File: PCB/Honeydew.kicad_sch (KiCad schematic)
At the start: 12 parts

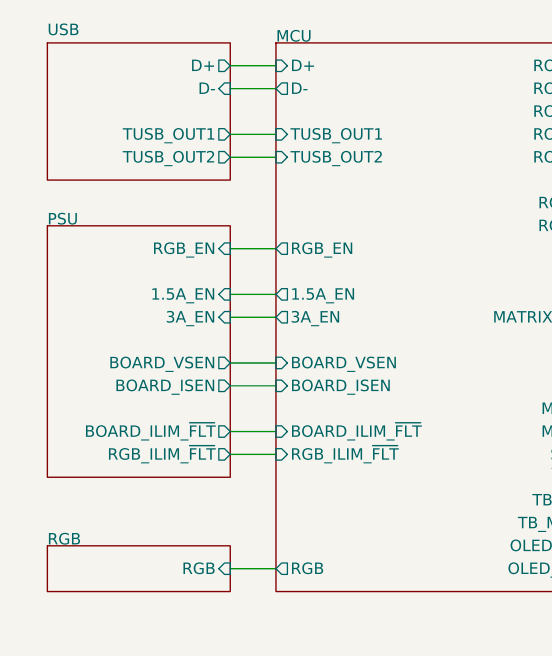
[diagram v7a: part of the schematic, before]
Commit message: Finished routing RGB LEDs.
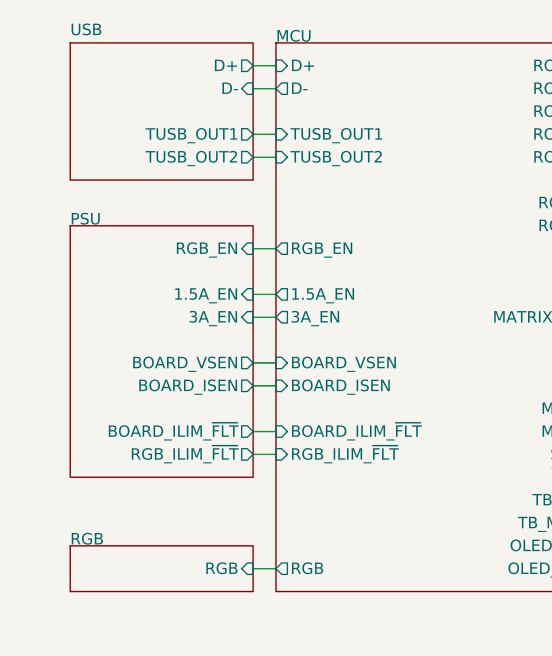
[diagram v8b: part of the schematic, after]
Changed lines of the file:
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@@
     (stroke (width 0) (type default))
   )
-  (wire (pts (xy 38.1 60.96) (xy 43.18 60.96))
+  (wire (pts (xy 40.64 60.96) (xy 43.18 60.96))
     (stroke (width 0) (type default))
   )
@@
     (stroke (width 0) (type default))
   )
-  (wire (pts (xy 38.1 76.2) (xy 43.18 76.2))
+  (wire (pts (xy 40.64 76.2) (xy 43.18 76.2))
     (stroke (width 0) (type default))
   )
@@
     (stroke (width 0) (type default))
   )
-  (wire (pts (xy 43.18 40.64) (xy 38.1 40.64))
+  (wire (pts (xy 43.18 40.64) (xy 40.64 40.64))
     (stroke (width 0) (type default))
   )
@@
     (stroke (width 0) (type default))
   )
-  (wire (pts (xy 43.18 20.32) (xy 38.1 20.32))
+  (wire (pts (xy 43.18 20.32) (xy 40.64 20.32))
     (stroke (width 0) (type default))
   )
@@
     (stroke (width 0) (type default))
   )
-  (wire (pts (xy 43.18 27.94) (xy 38.1 27.94))
+  (wire (pts (xy 43.18 27.94) (xy 40.64 27.94))
     (stroke (width 0) (type default))
   )
@@
     (stroke (width 0) (type default))
   )
-  (wire (pts (xy 38.1 48.26) (xy 43.18 48.26))
-    (stroke (width 0) (type default))
-  )
-  (wire (pts (xy 43.18 45.72) (xy 38.1 45.72))
-    (stroke (width 0) (type default))
-  )
-  (wire (pts (xy 38.1 22.86) (xy 43.18 22.86))
+  (wire (pts (xy 40.64 48.26) (xy 43.18 48.26))
+    (stroke (width 0) (type default))
+  )
+  (wire (pts (xy 43.18 45.72) (xy 40.64 45.72))
+    (stroke (width 0) (type default))
+  )
+  (wire (pts (xy 40.64 22.86) (xy 43.18 22.86))
     (stroke (width 0) (type default))
   )
@@
     (stroke (width 0) (type default))
   )
-  (wire (pts (xy 43.18 53.34) (xy 38.1 53.34))
-    (stroke (width 0) (type default))
-  )
-  (wire (pts (xy 38.1 63.5) (xy 43.18 63.5))
+  (wire (pts (xy 43.18 53.34) (xy 40.64 53.34))
+    (stroke (width 0) (type default))
+  )
+  (wire (pts (xy 40.64 63.5) (xy 43.18 63.5))
     (stroke (width 0) (type default))
   )
@@
     (stroke (width 0) (type default))
   )
-  (wire (pts (xy 38.1 30.48) (xy 43.18 30.48))
-    (stroke (width 0) (type default))
-  )
-  (wire (pts (xy 38.1 55.88) (xy 43.18 55.88))
+  (wire (pts (xy 40.64 30.48) (xy 43.18 30.48))
+    (stroke (width 0) (type default))
+  )
+  (wire (pts (xy 40.64 55.88) (xy 43.18 55.88))
     (stroke (width 0) (type default))
   )
@@
     )
   )
-  (sheet (at 17.78 17.78) (size 20.32 15.24) (fields_autoplaced)
+  (sheet (at 20.32 17.78) (size 20.32 15.24) (fields_autoplaced)
     (stroke (width 0.1524) (type solid))
     (fill (color 0 0 0 0.0000))
-    (property "Sheetname" "USB" (at 17.78 17.0684 0)
+    (property "Sheetname" "USB" (at 20.32 17.0684 0)
       (effects (font (size 1.27 1.27)) (justify left bottom))
     )
-    (property "Sheetfile" "USB.kicad_sch" (at 17.78 33.6046 0)
+    (property "Sheetfile" "USB.kicad_sch" (at 20.32 33.6046 0)
       (effects (font (size 1.27 1.27)) (justify left top) hide)
     )
-    (pin "D-" input (at 38.1 22.86 0)
-      (effects (font (size 1.27 1.27)) (justify right))
-    )
-    (pin "D+" output (at 38.1 20.32 0)
-      (effects (font (size 1.27 1.27)) (justify right))
-    )
-    (pin "TUSB_OUT1" output (at 38.1 27.94 0)
-      (effects (font (size 1.27 1.27)) (justify right))
-    )
-    (pin "TUSB_OUT2" output (at 38.1 30.48 0)
+    (pin "D-" input (at 40.64 22.86 0)
+      (effects (font (size 1.27 1.27)) (justify right))
+    )
+    (pin "D+" output (at 40.64 20.32 0)
+      (effects (font (size 1.27 1.27)) (justify right))
+    )
+    (pin "TUSB_OUT1" output (at 40.64 27.94 0)
+      (effects (font (size 1.27 1.27)) (justify right))
+    )
+    (pin "TUSB_OUT2" output (at 40.64 30.48 0)
       (effects (font (size 1.27 1.27)) (justify right))
     )
@@
     )
   )
-  (sheet (at 17.78 38.1) (size 20.32 27.94)
+  (sheet (at 20.32 38.1) (size 20.32 27.94)
     (stroke (width 0.1524) (type solid))
     (fill (color 0 0 0 0.0000))
-    (property "Sheetname" "PSU" (at 17.78 38.1 0)
+    (property "Sheetname" "PSU" (at 20.32 38.1 0)
       (effects (font (size 1.27 1.27)) (justify left bottom))
     )
-    (property "Sheetfile" "PSU.kicad_sch" (at 17.78 34.29 0)
+    (property "Sheetfile" "PSU.kicad_sch" (at 20.32 34.29 0)
       (effects (font (size 1.27 1.27)) (justify left) hide)
     )
-    (pin "BOARD_VSEN" output (at 38.1 53.34 0)
-      (effects (font (size 1.27 1.27)) (justify right))
-    )
-    (pin "BOARD_ILIM_~{FLT}" output (at 38.1 60.96 0)
-      (effects (font (size 1.27 1.27)) (justify right))
-    )
-    (pin "BOARD_ISEN" output (at 38.1 55.88 0)
-      (effects (font (size 1.27 1.27)) (justify right))
-    )
-    (pin "RGB_EN" input (at 38.1 40.64 0)
-      (effects (font (size 1.27 1.27)) (justify right))
-    )
-    (pin "3A_EN" input (at 38.1 48.26 0)
-      (effects (font (size 1.27 1.27)) (justify right))
-    )
-    (pin "1.5A_EN" input (at 38.1 45.72 0)
-      (effects (font (size 1.27 1.27)) (justify right))
-    )
-    (pin "RGB_ILIM_~{FLT}" output (at 38.1 63.5 0)
+    (pin "BOARD_VSEN" output (at 40.64 53.34 0)
+      (effects (font (size 1.27 1.27)) (justify right))
+    )
+    (pin "BOARD_ILIM_~{FLT}" output (at 40.64 60.96 0)
+      (effects (font (size 1.27 1.27)) (justify right))
+    )
+    (pin "BOARD_ISEN" output (at 40.64 55.88 0)
+      (effects (font (size 1.27 1.27)) (justify right))
+    )
+    (pin "RGB_EN" input (at 40.64 40.64 0)
+      (effects (font (size 1.27 1.27)) (justify right))
+    )
+    (pin "3A_EN" input (at 40.64 48.26 0)
+      (effects (font (size 1.27 1.27)) (justify right))
+    )
+    (pin "1.5A_EN" input (at 40.64 45.72 0)
+      (effects (font (size 1.27 1.27)) (justify right))
+    )
+    (pin "RGB_ILIM_~{FLT}" output (at 40.64 63.5 0)
       (effects (font (size 1.27 1.27)) (justify right))
     )
@@
     )
   )
-  (sheet (at 17.78 73.66) (size 20.32 5.08)
+  (sheet (at 20.32 73.66) (size 20.32 5.08)
     (stroke (width 0.1524) (type solid))
     (fill (color 0 0 0 0.0000))
-    (property "Sheetname" "RGB" (at 17.78 73.66 0)
+    (property "Sheetname" "RGB" (at 20.32 73.66 0)
       (effects (font (size 1.27 1.27)) (justify left bottom))
     )
-    (property "Sheetfile" "RGB.kicad_sch" (at 36.1446 93.98 90)
+    (property "Sheetfile" "RGB.kicad_sch" (at 38.6846 93.98 90)
       (effects (font (size 1.27 1.27)) (justify left top) hide)
     )
-    (pin "RGB" input (at 38.1 76.2 0)
-      (effects (font (size 1.27 1.27)) (justify right))
-    )
+    (pin "RGB" input (at 40.64 76.2 0)
+      (effects (font (size 1.27 1.27)) (justify right))
+    )
